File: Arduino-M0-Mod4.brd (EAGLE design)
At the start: 68.6 x 53.3 mm, 116 parts, among them CN2 PINHEAD-2x5-P1.27, IC1 74LVC1G125DCKR, IC2 SAMD21G18A-AUT, IC3 MPM3610, IC4 MPM3810GQB-33, IC5 RTC_PCF8523T, IC6 EM4095, Y1 32.768kHz, Y4 32,768Khz

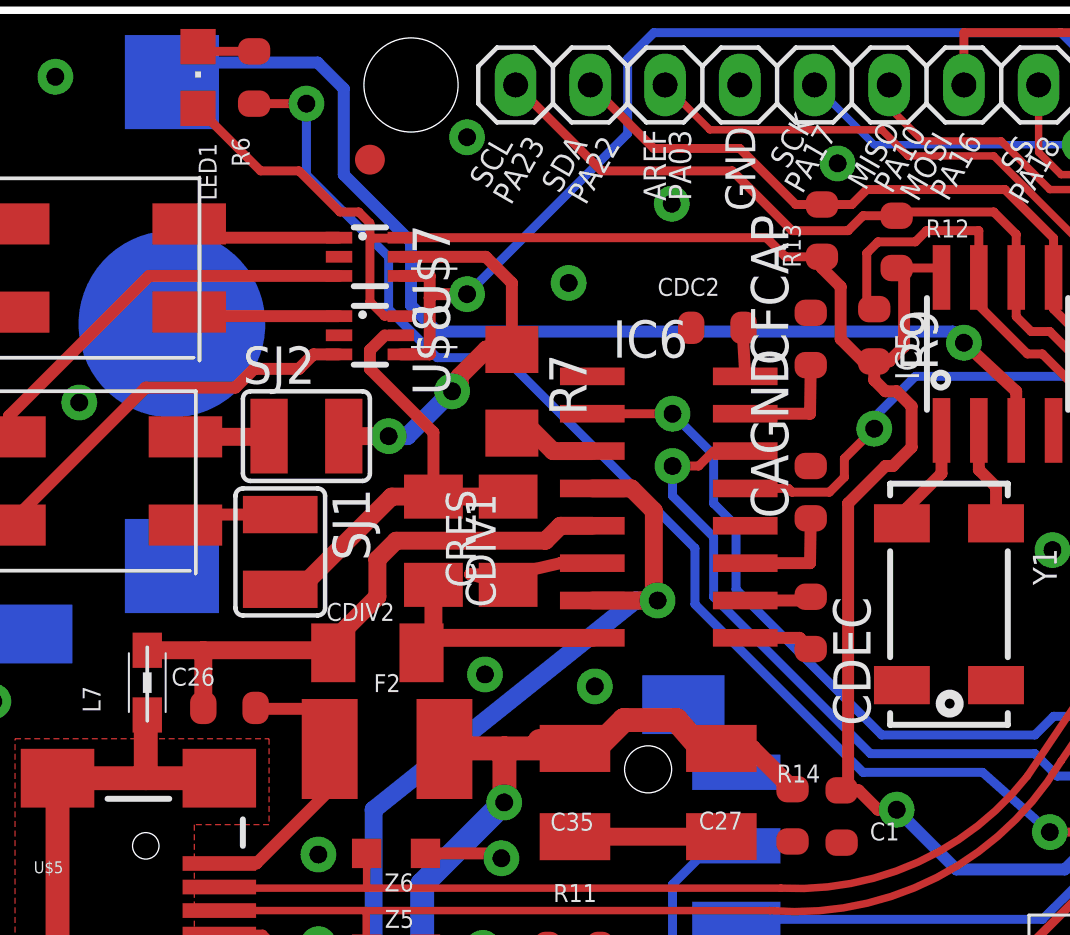
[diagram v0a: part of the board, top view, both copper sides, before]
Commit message: Conceptual prototype 2 minor board edits
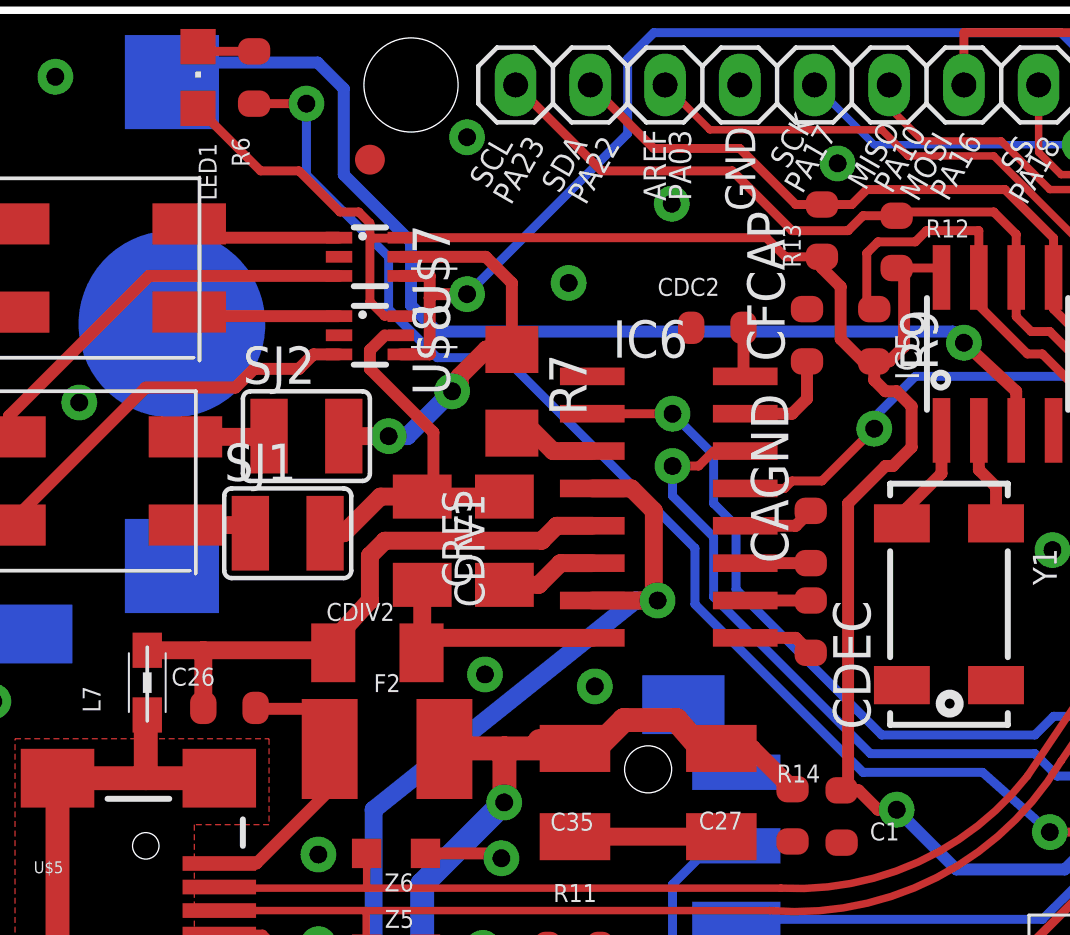
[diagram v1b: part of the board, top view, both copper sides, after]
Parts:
- moved CAGND 1.52 mm to (28.8, 35.4)
- moved SJ1 0.68 mm to (11.0, 35.6), turned to 0 degrees
- moved CDIV1 0.38 mm to (15.6, 35.3)
- moved CFCAP 0.18 mm to (28.7, 42.3)
- moved CDEC 0.13 mm to (28.8, 32.4)
- moved CRES 0.13 mm to (18.4, 35.3)
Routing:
- net GND: track 129.0 -> 131.7 mm
- net N$16: track 16.2 -> 13.9 mm
- net N$12: track 5.54 -> 3.29 mm
- net N$5: track 3.73 -> 2.23 mm
- net N$21: track 17.1 -> 16.6 mm
